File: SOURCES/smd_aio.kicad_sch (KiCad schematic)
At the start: 86 parts, among them J1 RCA_01, J2 RCA_01, J5 Conn_01x02, J6 Conn_01x02, P1 MUTE, P16 TST, P2 CONN_01X04, P23 TST, P3 CONN_01X03, P32 /SD, P33 GP4, P34 GP5, P35 GP6, P4 CONN_02X05 Boxed, P5 STDCONN, P6 CONN_02X04, P7 CONN_02X04, P8 CONN_02X04, SW1 SW_PUSH, U1 ADAU1701, U13 OP279, U2 24AA256SN, U3 SN74LVC14ADG4, U8 MCP23008-xSS

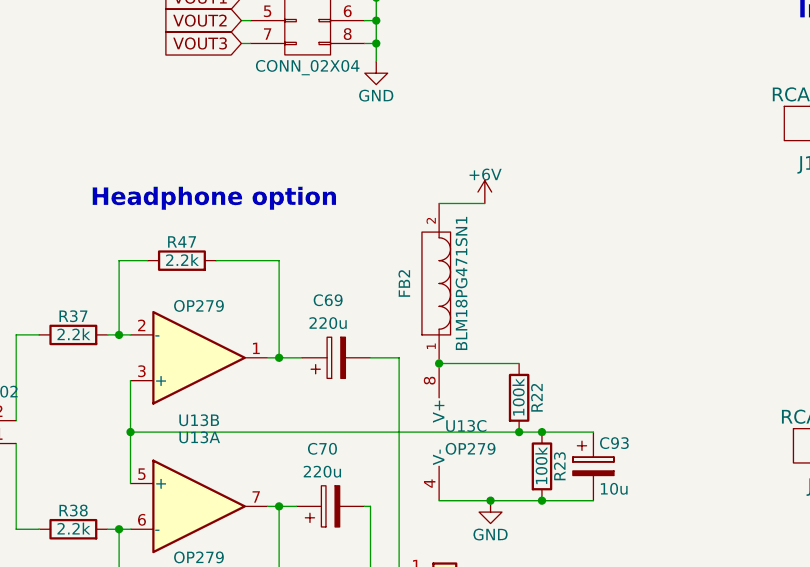
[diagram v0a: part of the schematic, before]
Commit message: Cleaned up ground plane under amps.
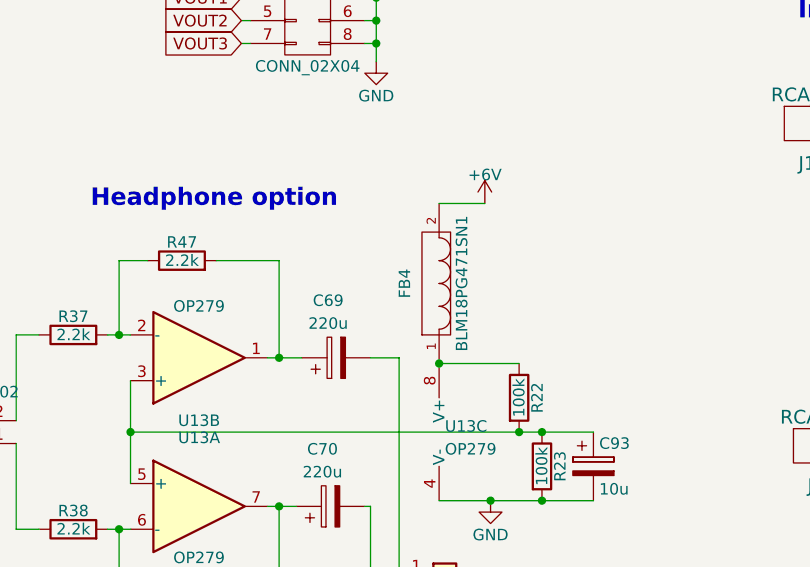
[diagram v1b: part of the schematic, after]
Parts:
- renumbered FB2 to FB4

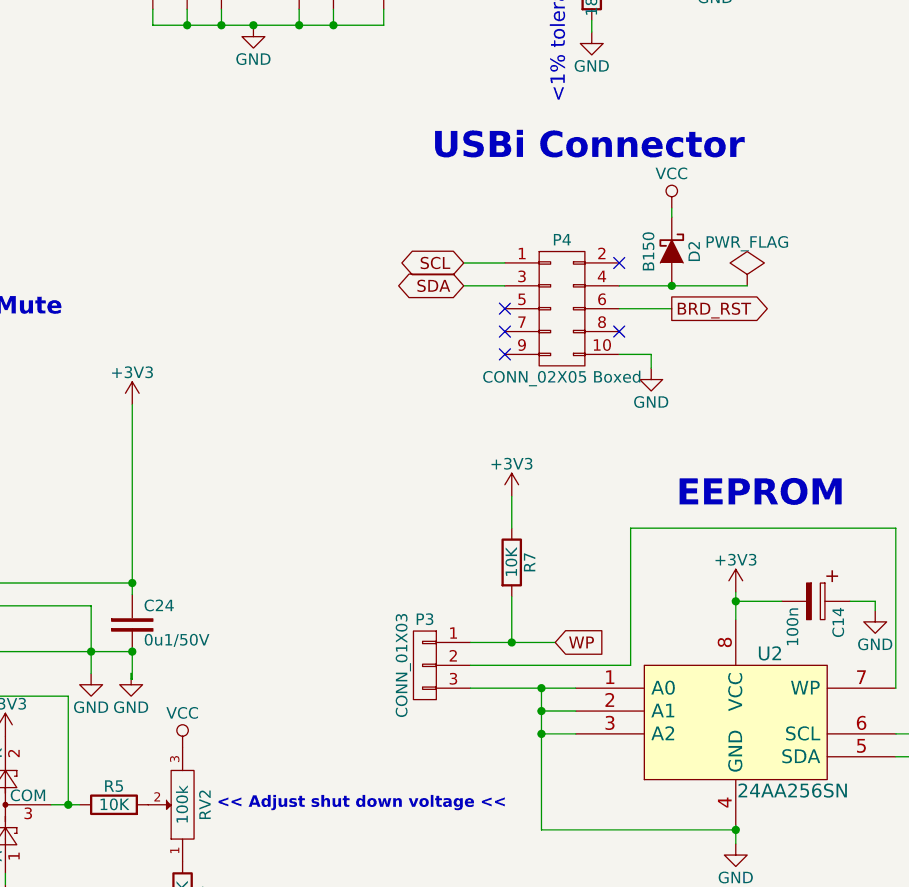
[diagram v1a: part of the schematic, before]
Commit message: Fixed Vin/Vcc issue.
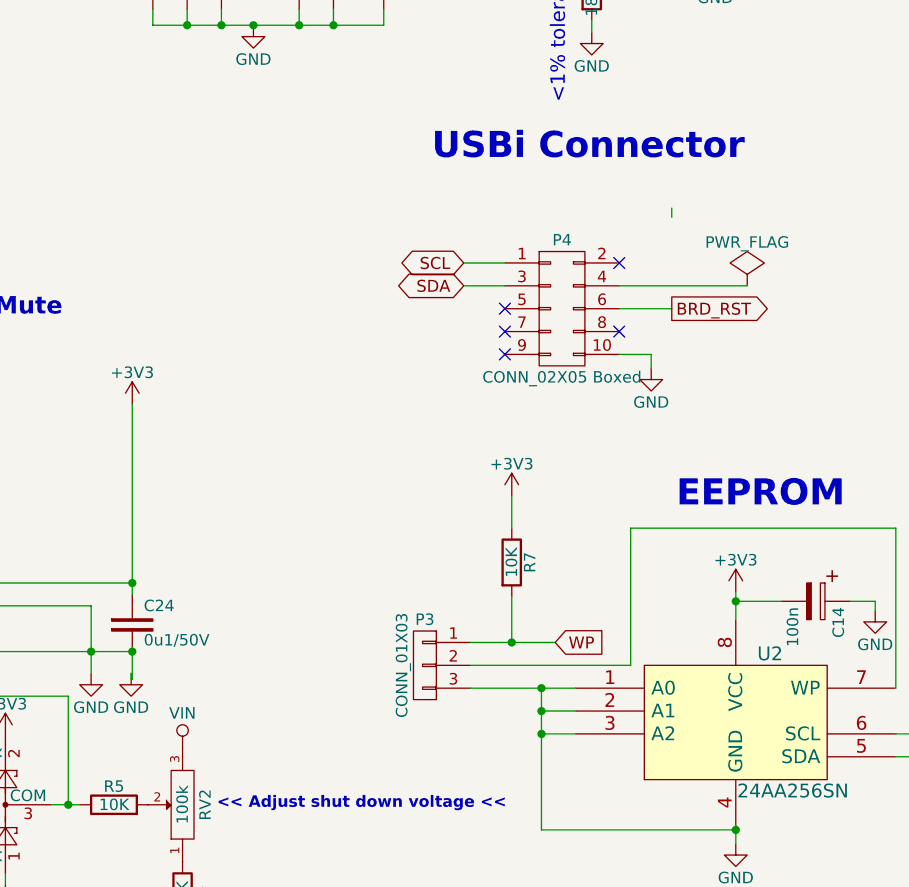
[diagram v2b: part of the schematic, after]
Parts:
- removed D2: B150, fdsp_diode:SMA, symbol smd_aio-rescue:D_Schottky
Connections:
- net VCC is gone; now on net VIN: RV2.3
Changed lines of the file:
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@@
 	)
 	(junction
-		(at 143.256 144.272)
-		(diameter 0)
-		(color 0 0 0 0)
-	)
-	(junction
 		(at 39.116 212.598)
 		(diameter 0)
@@
 	(wire
 		(pts
-			(xy 143.256 144.272) (xy 151.638 144.272)
-		)
-		(stroke
-			(width 0)
-			(type default)
-		)
-	)
-	(wire
-		(pts
 			(xy 164.084 103.886) (xy 168.148 103.886)
 		)
@@
 	(wire
 		(pts
-			(xy 137.414 144.272) (xy 143.256 144.272)
+			(xy 137.414 144.272) (xy 151.638 144.272)
 		)
 		(stroke
@@
 	)
 	(symbol
-		(lib_id "smd_aio-rescue:D_Schottky")
-		(at 143.256 140.462 270)
-		(unit 1)
-		(exclude_from_sim no)
-		(in_bom yes)
-		(on_board yes)
-		(dnp no)
-		(property "Reference" "D2"
-			(at 145.796 140.462 0)
-			(effects
-				(font
-					(size 1.27 1.27)
-				)
-			)
-		)
-		(property "Value" "B150"
-			(at 140.716 140.462 0)
-			(effects
-				(font
-					(size 1.27 1.27)
-				)
-			)
-		)
-		(property "Footprint" "fdsp_diode:SMA"
-			(at 143.256 140.462 0)
-			(effects
-				(font
-					(size 1.27 1.27)
-				)
-				(hide yes)
-			)
-		)
-		(property "Datasheet" ""
-			(at 143.256 140.462 0)
-			(effects
-				(font
-					(size 1.27 1.27)
-				)
-				(hide yes)
-			)
-		)
-		(property "Description" ""
-			(at 143.256 140.462 0)
-			(effects
-				(font
-					(size 1.27 1.27)
-				)
-				(hide yes)
-			)
-		)
-		(pin "1"
-		)
-		(pin "2"
-		)
-		(instances
-			(project "smd_aio"
-				(path "/4c49a07c-9ad4-4758-901a-e68e360dc17d"
-					(reference "D2")
-					(unit 1)
-				)
-			)
-		)
-	)
-	(symbol
 		(lib_id "smd_aio-rescue:PWR_FLAG")
 		(at 151.638 144.272 0)
@@
 	)
 	(symbol
-		(lib_id "smd_aio-rescue:VCC")
-		(at 143.256 135.636 0)
-		(unit 1)
-		(exclude_from_sim no)
-		(in_bom yes)
-		(on_board yes)
-		(dnp no)
-		(property "Reference" "#PWR039"
-			(at 143.256 139.446 0)
-			(effects
-				(font
-					(size 1.27 1.27)
-				)
-				(hide yes)
-			)
-		)
-		(property "Value" "VCC"
-			(at 143.256 131.826 0)
-			(effects
-				(font
-					(size 1.27 1.27)
-				)
-			)
-		)
-		(property "Footprint" ""
-			(at 143.256 135.636 0)
-			(effects
-				(font
-					(size 1.524 1.524)
-				)
-			)
-		)
-		(property "Datasheet" ""
-			(at 143.256 135.636 0)
-			(effects
-				(font
-					(size 1.524 1.524)
-				)
-			)
-		)
-		(property "Description" ""
-			(at 143.256 135.636 0)
-			(effects
-				(font
-					(size 1.27 1.27)
-				)
-				(hide yes)
-			)
-		)
-		(pin "1"
-		)
-		(instances
-			(project "smd_aio"
-				(path "/4c49a07c-9ad4-4758-901a-e68e360dc17d"
-					(reference "#PWR039")
-					(unit 1)
-				)
-			)
-		)
-	)
-	(symbol
 		(lib_id "smd_aio-rescue:CONN_02X04")
 		(at 262.89 150.495 0)
@@
 			)
 		)
-		(property "Value" "VCC"
+		(property "Value" "VIN"
 			(at 88.9 191.77 0)
 			(effects

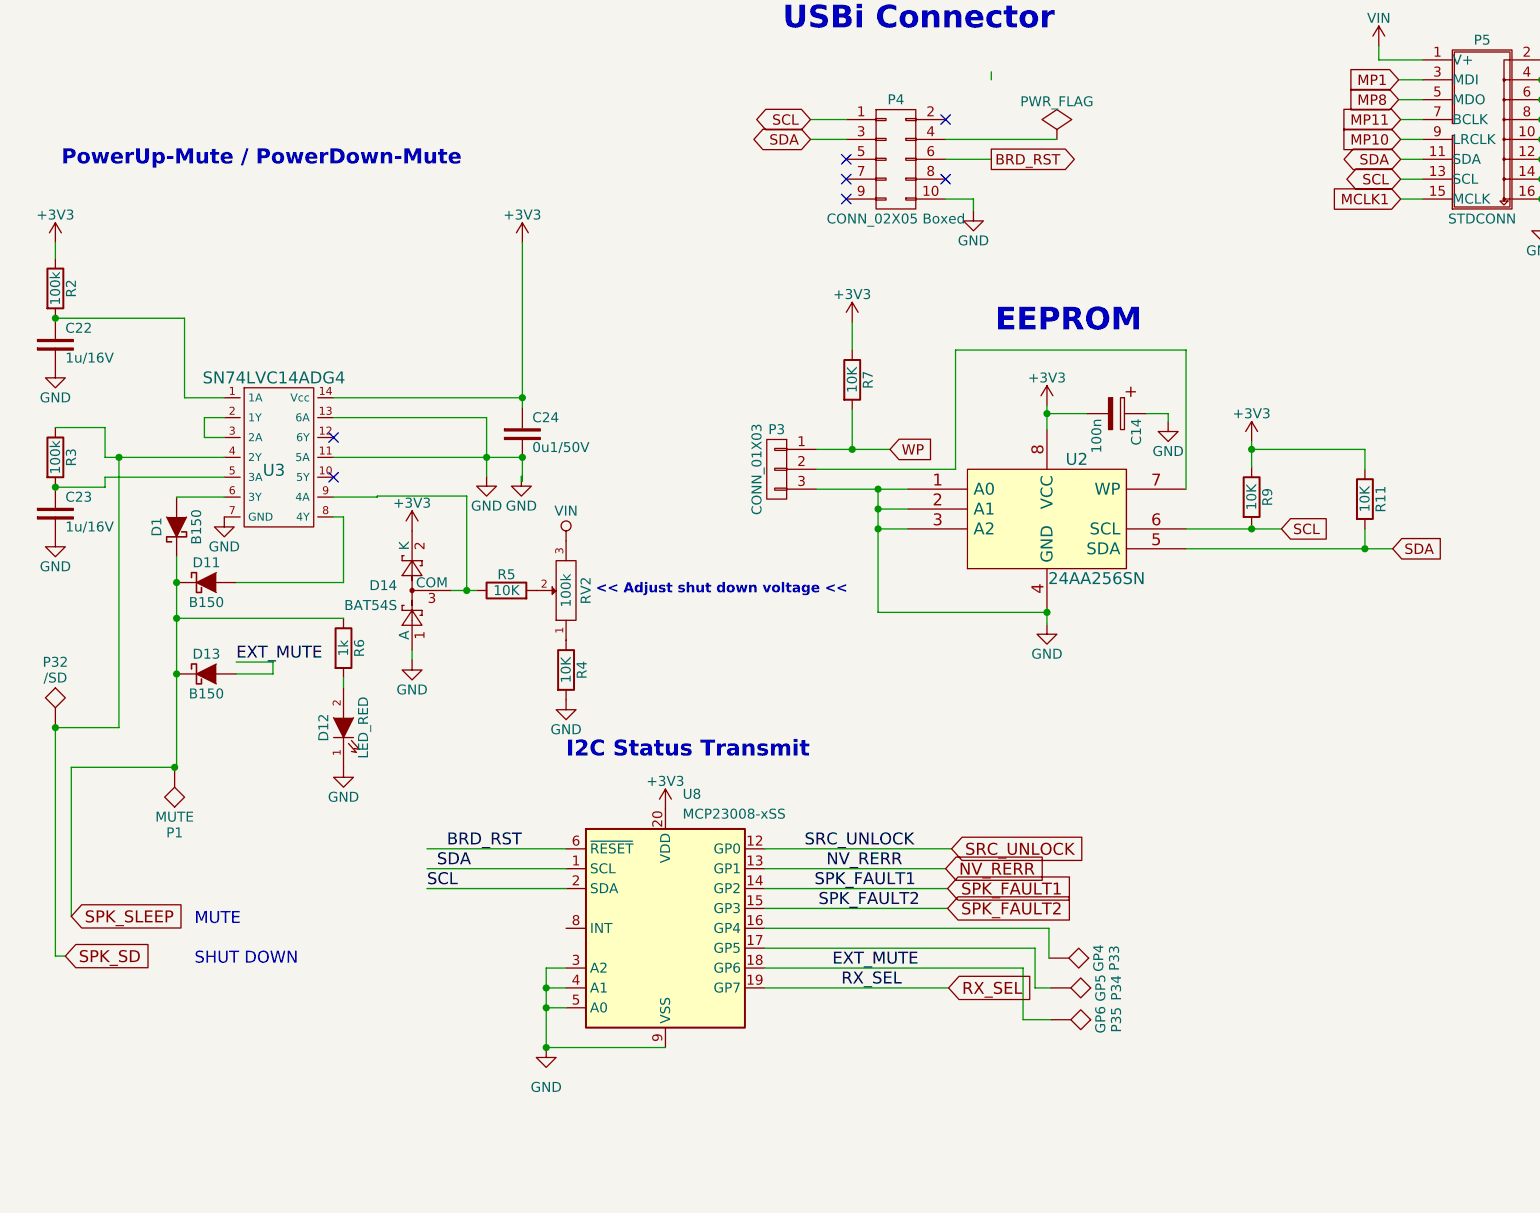
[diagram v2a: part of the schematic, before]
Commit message: Improved power traces.
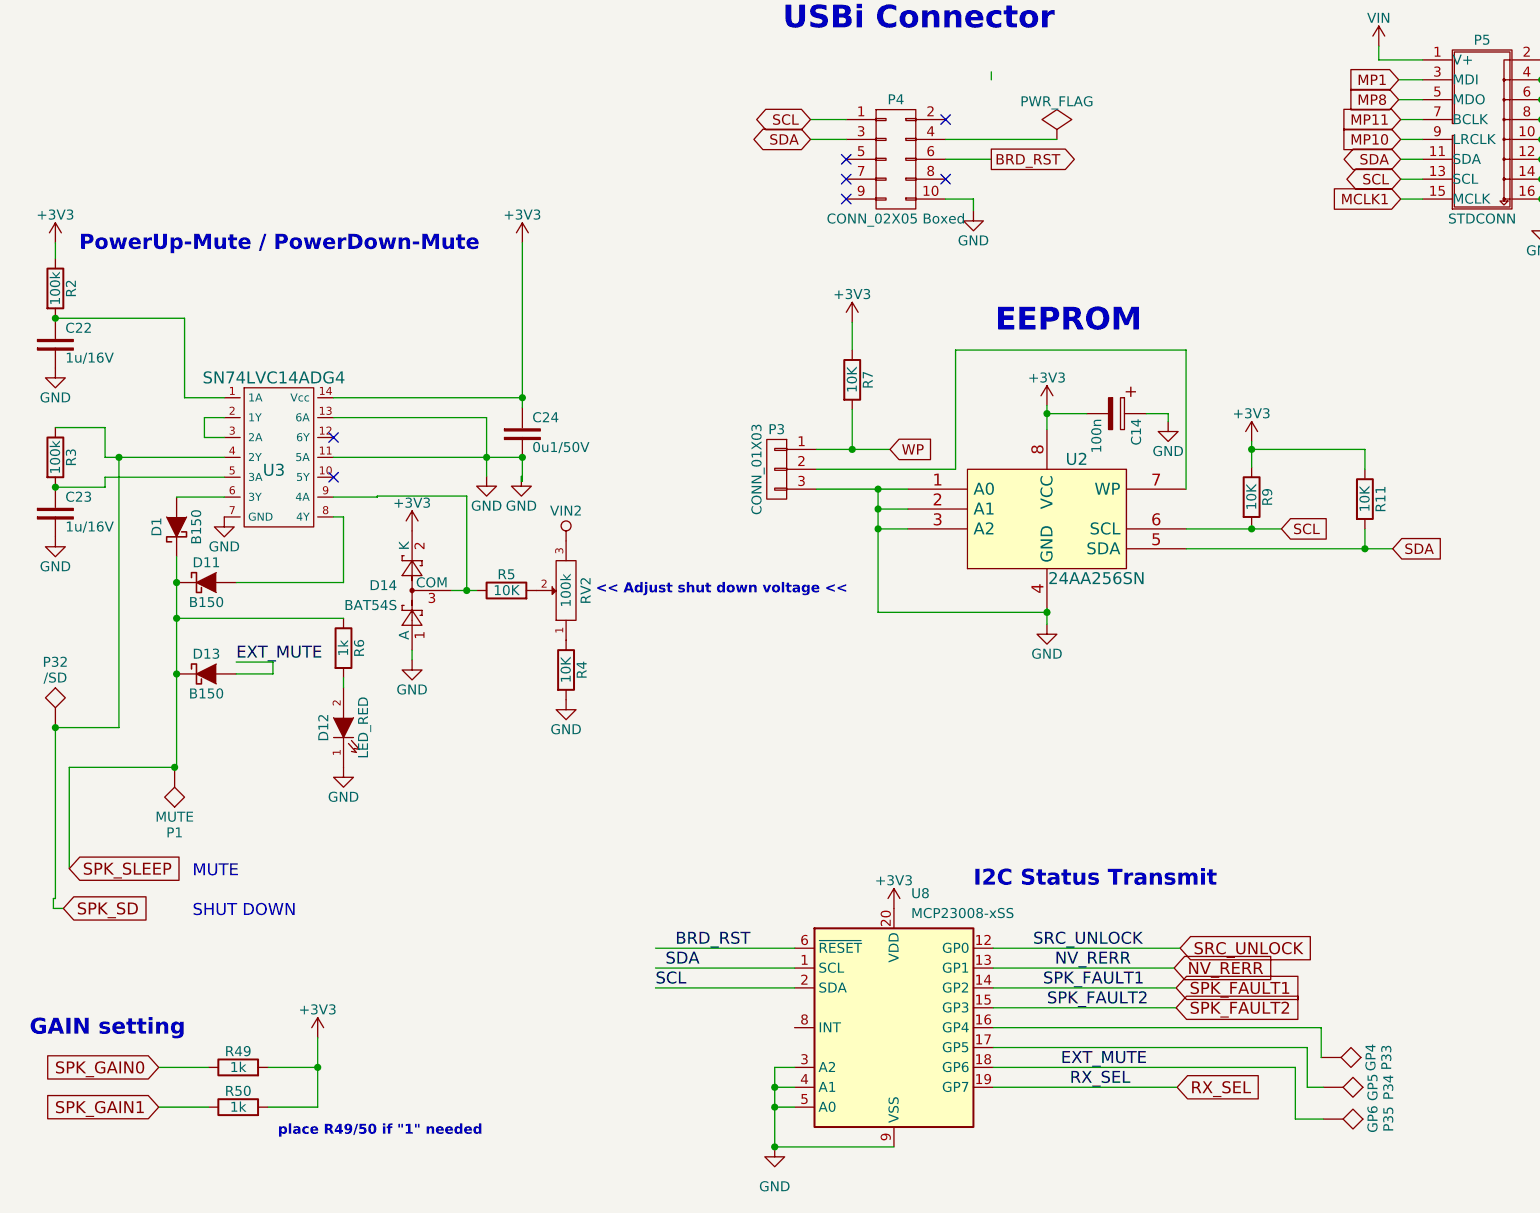
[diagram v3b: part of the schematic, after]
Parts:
- added R49, R50: 1k, Resistor_SMD:R_0603_1608Metric_Pad0.98x0.95mm_HandSolder, symbol Device:R
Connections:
- net +3V3: now also R49.2, R50.2
- net VIN: no longer RV2.3
- new net SPK_GAIN0: R49.1
- new net SPK_GAIN1: R50.1
- new net VIN2: RV2.3
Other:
- note added: "GAIN setting"
- note added: "place R49/50 if "1" needed"
- moved on the sheet: P33, P34, P35, U8

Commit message: Made some space for under side heat sink.. todo, move the WP jumper.
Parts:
- C2: footprint fdsp_capacitor:C_Radial_D5_L11_P2 -> Capacitor_SMD:C_1210_3225Metric_Pad1.33x2.70mm_HandSolder
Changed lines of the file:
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@@
 			)
 		)
-		(property "Footprint" "fdsp_capacitor:C_Radial_D5_L11_P2"
+		(property "Footprint" "Capacitor_SMD:C_1210_3225Metric_Pad1.33x2.70mm_HandSolder"
 			(at 78.486 31.4452 0)
 			(effects
